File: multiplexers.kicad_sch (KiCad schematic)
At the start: 6 parts, among them U2 74HC4067, U3 74HC4067, U4 74HC4067, U5 74HC4067, U6 74HC4067, U7 74HC4067

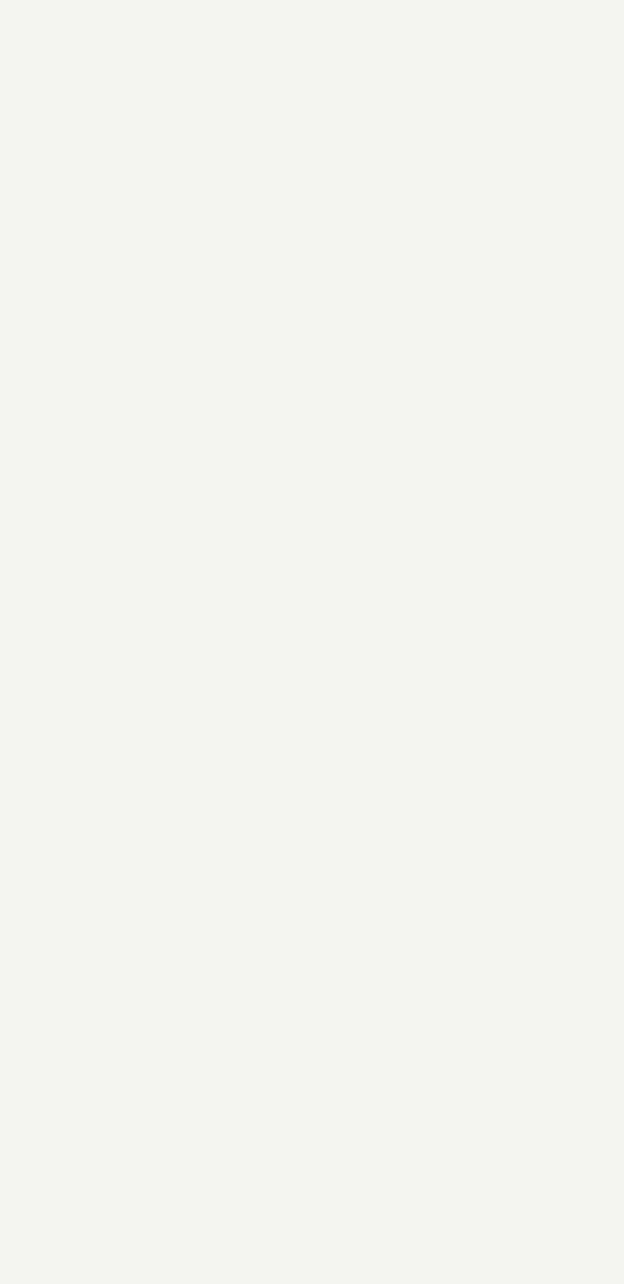
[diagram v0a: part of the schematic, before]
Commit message: Added All the Keyswitches Required
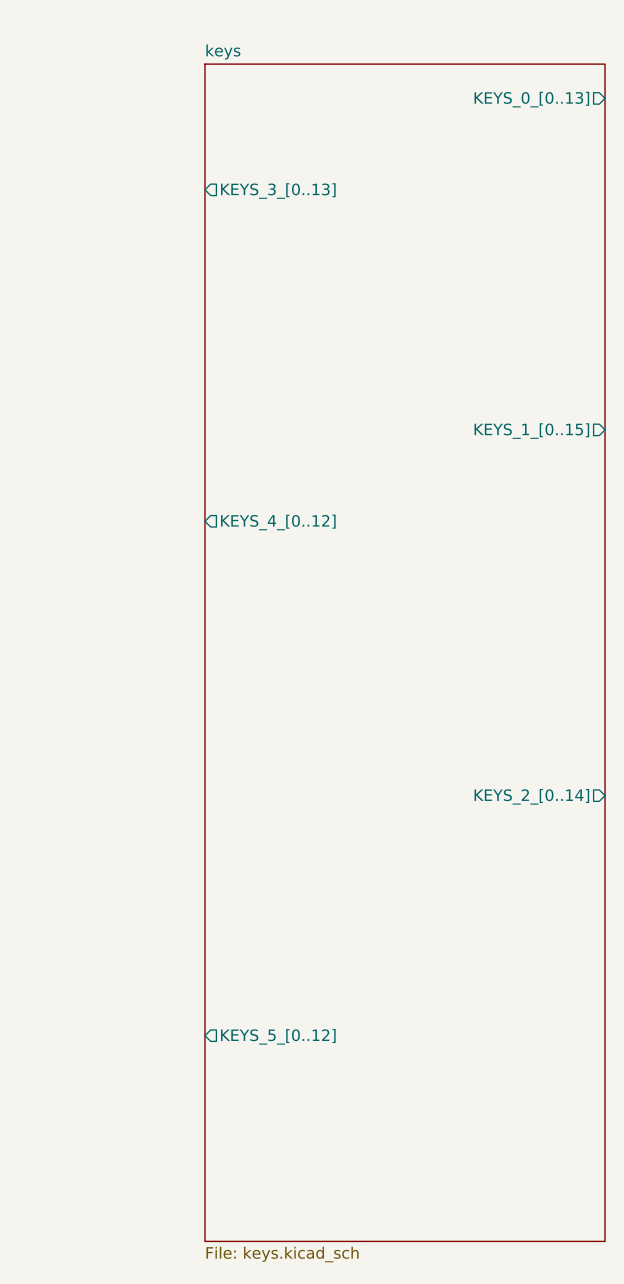
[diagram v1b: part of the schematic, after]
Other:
- added sheet keys (keys.kicad_sch)
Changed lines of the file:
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@@
+    )
+  )
+  (sheet (at 217.17 24.13) (size 44.45 130.81) (fields_autoplaced)
+    (stroke (width 0.1524) (type solid))
+    (fill (color 0 0 0 0.0000))
+    (property "Sheetname" "keys" (at 217.17 23.4184 0)
+      (effects (font (size 1.27 1.27)) (justify left bottom))
+    )
+    (property "Sheetfile" "keys.kicad_sch" (at 217.17 155.5246 0)
+      (effects (font (size 1.27 1.27)) (justify left top))
+    )
+    (pin "KEYS_0_[0..13]" output (at 261.62 27.94 0)
+      (effects (font (size 1.27 1.27)) (justify right))
+    )
+    (pin "KEYS_5_[0..12]" output (at 217.17 132.08 180)
+      (effects (font (size 1.27 1.27)) (justify left))
+    )
+    (pin "KEYS_2_[0..14]" output (at 261.62 105.41 0)
+      (effects (font (size 1.27 1.27)) (justify right))
+    )
+    (pin "KEYS_3_[0..13]" output (at 217.17 38.1 180)
+      (effects (font (size 1.27 1.27)) (justify left))
+    )
+    (pin "KEYS_1_[0..15]" output (at 261.62 64.77 0)
+      (effects (font (size 1.27 1.27)) (justify right))
+    )
+    (pin "KEYS_4_[0..12]" output (at 217.17 74.93 180)
+      (effects (font (size 1.27 1.27)) (justify left))
+    )
+    (instances
+      (project "Erebus"
+        (path "/d88b0230-c6e0-4e9b-98a2-e29afd320bb6/a87a9230-372e-45a2-97eb-0c46b92f006f" (page "3"))
+      )
     )
   )

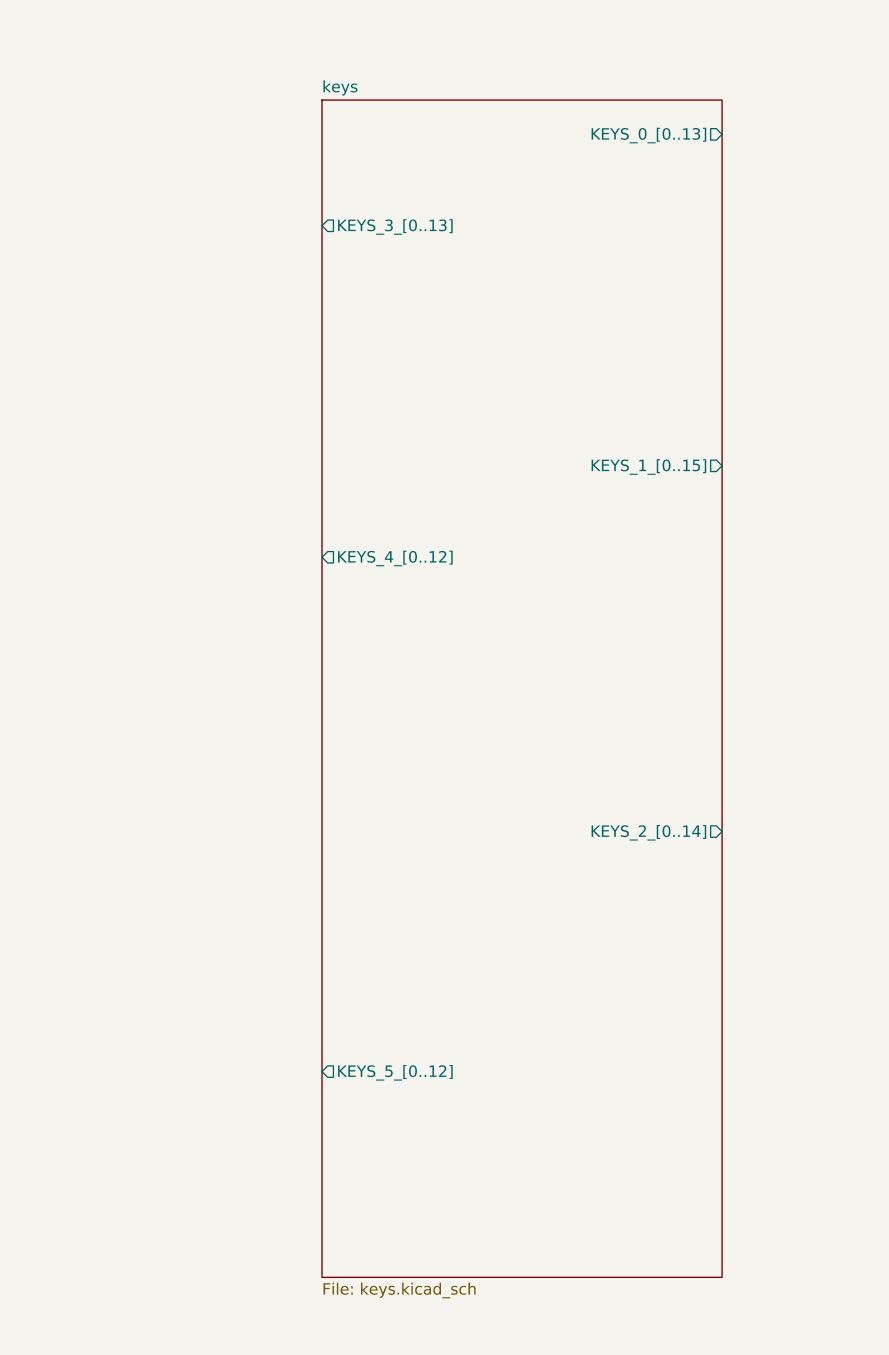
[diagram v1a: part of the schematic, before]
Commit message: Added Extra B and Started Multiplexer Layout
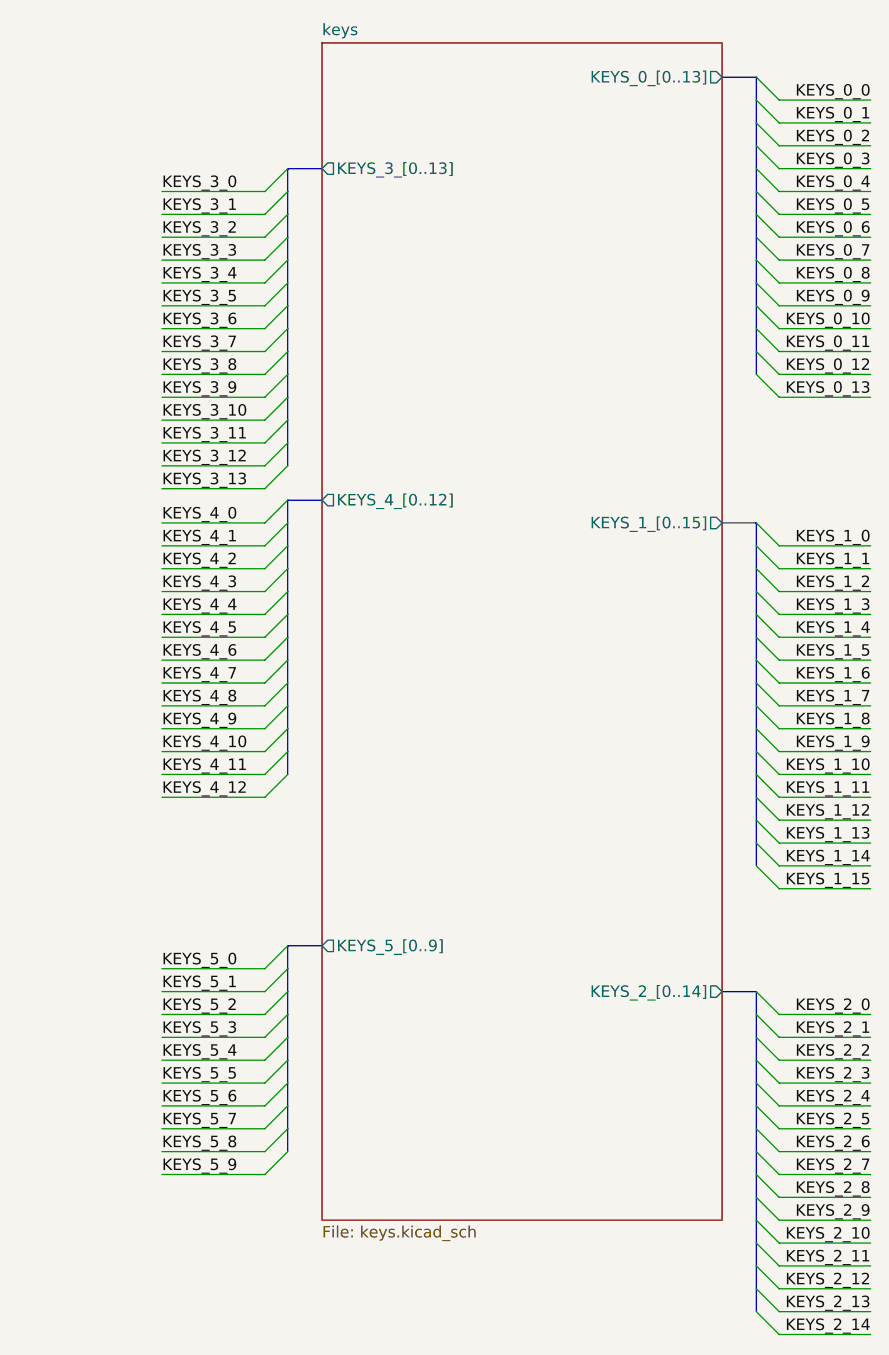
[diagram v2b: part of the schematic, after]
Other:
- sheet keys ports: added KEYS_5_[0..9]; removed KEYS_5_[0..12]

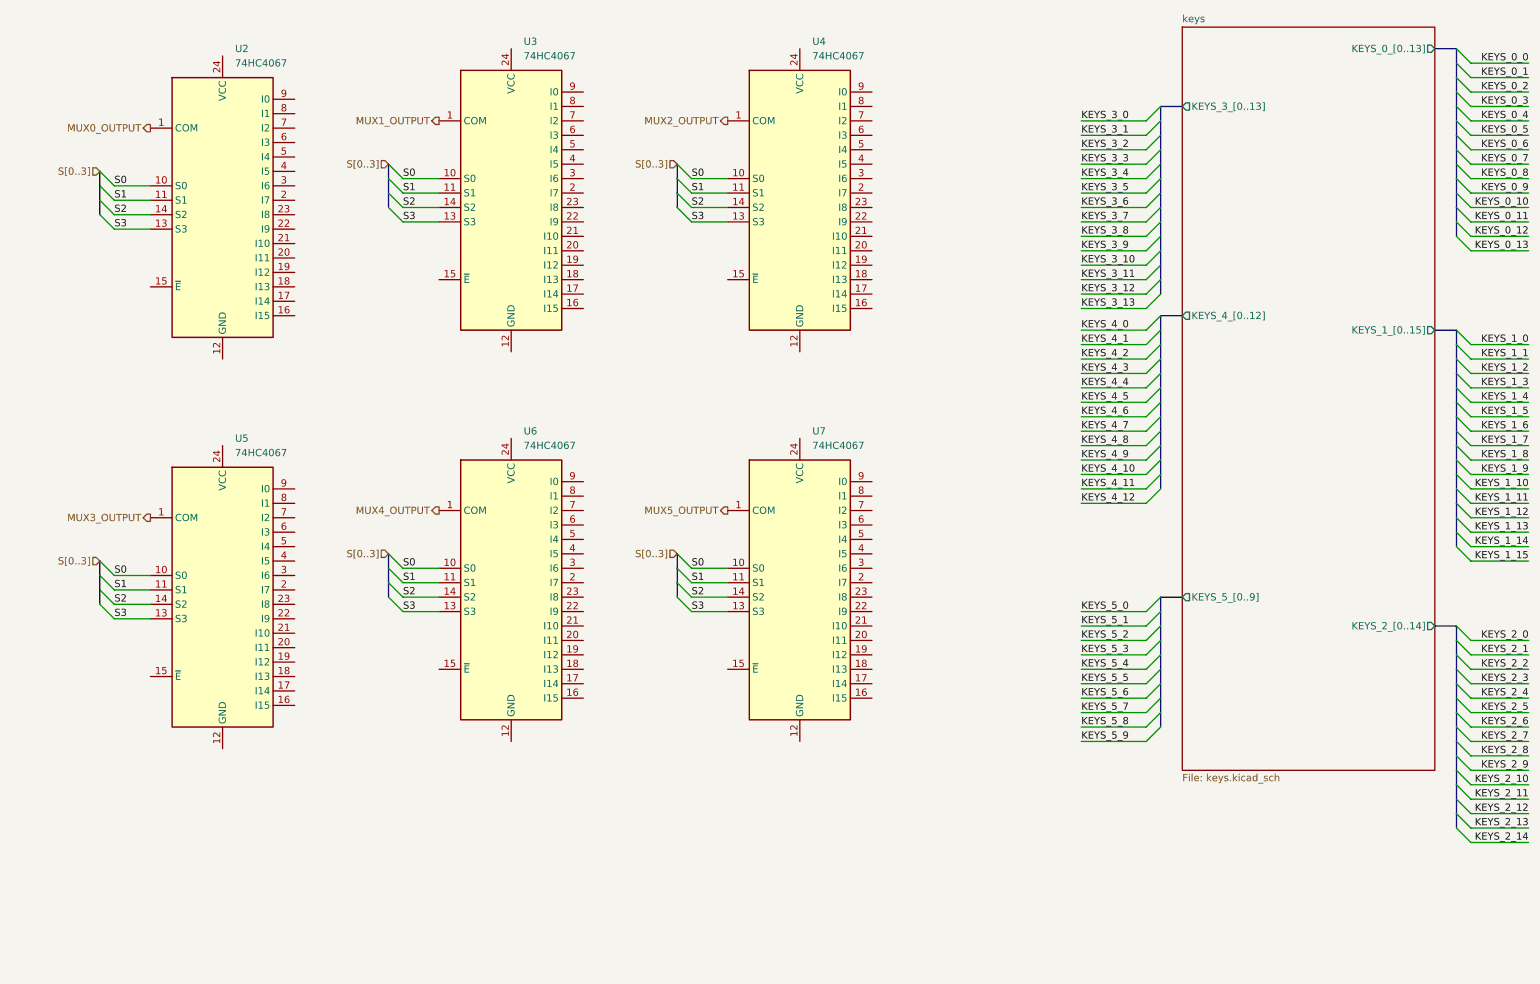
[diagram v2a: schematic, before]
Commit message: Added All Keys to Multiplexers
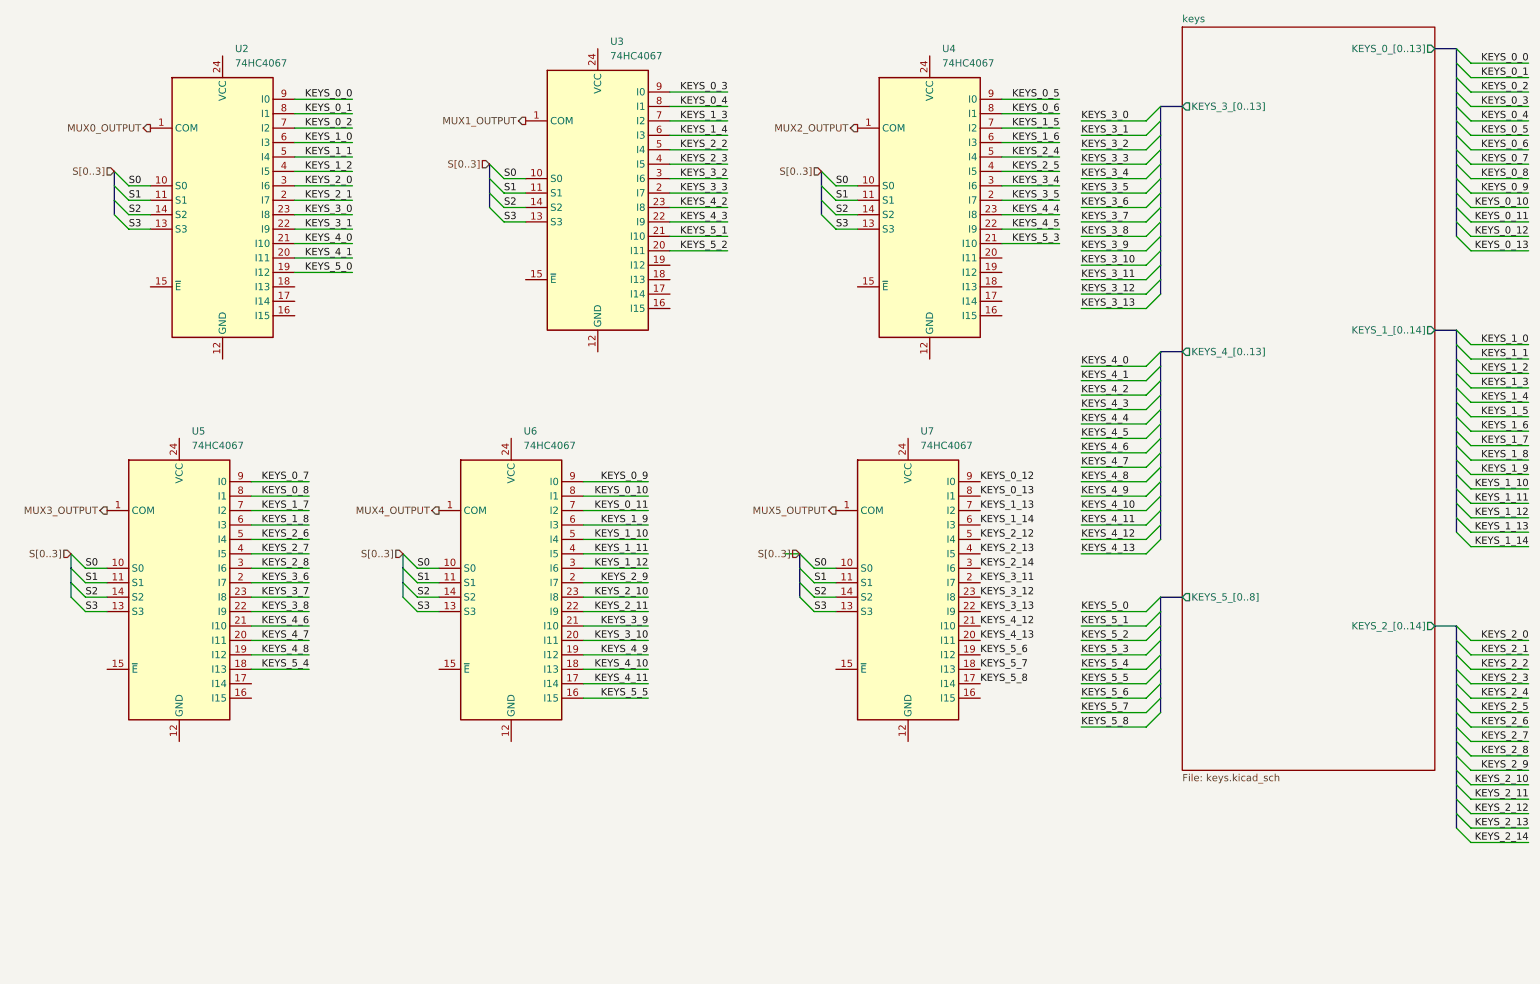
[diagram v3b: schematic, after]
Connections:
- net KEYS_0_0: now also U2.9 (I0)
- net KEYS_0_1: now also U2.8 (I1)
- net KEYS_0_10: now also U6.8 (I1)
- net KEYS_0_11: now also U6.7 (I2)
- net KEYS_0_12: now also U7.9 (I0)
- net KEYS_0_13: now also U7.8 (I1)
- net KEYS_0_2: now also U2.7 (I2)
- net KEYS_0_3: now also U3.9 (I0)
- net KEYS_0_4: now also U3.8 (I1)
- net KEYS_0_5: now also U4.9 (I0)
- net KEYS_0_6: now also U4.8 (I1)
- net KEYS_0_7: now also U5.9 (I0)
- net KEYS_0_8: now also U5.8 (I1)
- net KEYS_0_9: now also U6.9 (I0)
- net KEYS_1_0: now also U2.6 (I3)
- net KEYS_1_1: now also U2.5 (I4)
- net KEYS_1_10: now also U6.5 (I4)
- net KEYS_1_11: now also U6.4 (I5)
- net KEYS_1_12: now also U6.3 (I6)
- net KEYS_1_13: now also U7.7 (I2)
- net KEYS_1_14: now also U7.6 (I3)
- net KEYS_1_2: now also U2.4 (I5)
- net KEYS_1_3: now also U3.7 (I2)
- net KEYS_1_4: now also U3.6 (I3)
- net KEYS_1_5: now also U4.7 (I2)
- net KEYS_1_6: now also U4.6 (I3)
- net KEYS_1_7: now also U5.7 (I2)
- net KEYS_1_8: now also U5.6 (I3)
- net KEYS_1_9: now also U6.6 (I3)
- net KEYS_2_0: now also U2.3 (I6)
- net KEYS_2_1: now also U2.2 (I7)
- net KEYS_2_10: now also U6.23 (I8)
- net KEYS_2_11: now also U6.22 (I9)
- net KEYS_2_12: now also U7.5 (I4)
- net KEYS_2_13: now also U7.4 (I5)
- net KEYS_2_14: now also U7.3 (I6)
- net KEYS_2_2: now also U3.5 (I4)
- net KEYS_2_3: now also U3.4 (I5)
- net KEYS_2_4: now also U4.5 (I4)
- net KEYS_2_5: now also U4.4 (I5)
- net KEYS_2_6: now also U5.5 (I4)
- net KEYS_2_7: now also U5.4 (I5)
- net KEYS_2_8: now also U5.3 (I6)
- net KEYS_2_9: now also U6.2 (I7)
- net KEYS_3_0: now also U2.23 (I8)
- net KEYS_3_1: now also U2.22 (I9)
- net KEYS_3_10: now also U6.20 (I11)
- net KEYS_3_11: now also U7.2 (I7)
- net KEYS_3_12: now also U7.23 (I8)
- net KEYS_3_13: now also U7.22 (I9)
- net KEYS_3_2: now also U3.3 (I6)
- net KEYS_3_3: now also U3.2 (I7)
- net KEYS_3_4: now also U4.3 (I6)
- net KEYS_3_5: now also U4.2 (I7)
- net KEYS_3_6: now also U5.2 (I7)
- net KEYS_3_7: now also U5.23 (I8)
- net KEYS_3_8: now also U5.22 (I9)
- net KEYS_3_9: now also U6.21 (I10)
- net KEYS_4_0: now also U2.21 (I10)
- net KEYS_4_1: now also U2.20 (I11)
- net KEYS_4_10: now also U6.18 (I13)
- net KEYS_4_11: now also U6.17 (I14)
- net KEYS_4_12: now also U7.21 (I10)
- net KEYS_4_2: now also U3.23 (I8)
- net KEYS_4_3: now also U3.22 (I9)
- net KEYS_4_4: now also U4.23 (I8)
- net KEYS_4_5: now also U4.22 (I9)
- net KEYS_4_6: now also U5.21 (I10)
- net KEYS_4_7: now also U5.20 (I11)
- net KEYS_4_8: now also U5.19 (I12)
- net KEYS_4_9: now also U6.19 (I12)
- net KEYS_5_0: now also U2.19 (I12)
- net KEYS_5_1: now also U3.21 (I10)
- net KEYS_5_2: now also U3.20 (I11)
- net KEYS_5_3: now also U4.21 (I10)
- net KEYS_5_4: now also U5.18 (I13)
- net KEYS_5_5: now also U6.16 (I15)
- net KEYS_5_6: now also U7.19 (I12)
- net KEYS_5_7: now also U7.18 (I13)
- net KEYS_5_8: now also U7.17 (I14)
- net KEYS_4_13: now reaches U7.20 (I11)
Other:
- sheet keys ports: added KEYS_1_[0..14], KEYS_4_[0..13], KEYS_5_[0..8]; removed KEYS_1_[0..15], KEYS_4_[0..12], KEYS_5_[0..9]
- moved on the sheet: U3, U4, U5, U7

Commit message: Setup Base Layout
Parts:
- added C1, C2, C3, C4, C5, C6: 100n, Capacitor_SMD:C_0402_1005Metric, symbol Device:C_Small
- renumbered U3 to U2, U2 to U3
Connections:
- net GND: now reaches U6.12 (GND)
- net GND: now also U2.12 (GND), U2.15 (~{E}), U3.12 (GND), U3.15 (~{E}), U4.12 (GND), U4.15 (~{E}), U5.12 (GND), U5.15 (~{E}), U6.15 (~{E}), U7.12 (GND), U7.15 (~{E}), C1.2, C2.2, C3.2, C4.2, C5.2, C6.2
- net +3V3: now reaches U6.24 (VCC)
- net +3V3: now also U2.24 (VCC), U3.24 (VCC), U4.24 (VCC), U5.24 (VCC), U7.24 (VCC), C1.1, C2.1, C3.1, C4.1, C5.1, C6.1
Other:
- note added: "Mux decoupling"
